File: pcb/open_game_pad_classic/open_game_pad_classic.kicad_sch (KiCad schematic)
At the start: 36 parts, among them J1 COM-09032, J2 COM-09032, J3 USB_C_Receptacle_USB2.0_14P, U1 MM74C923, U2 74HC4051

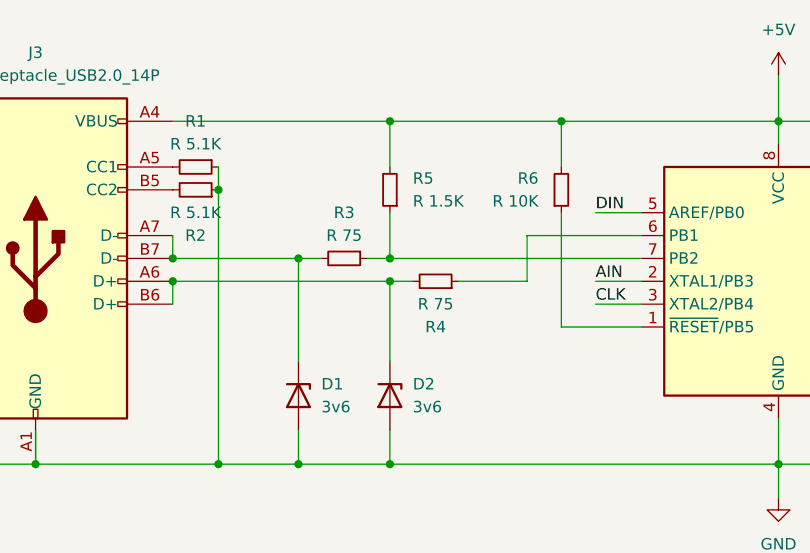
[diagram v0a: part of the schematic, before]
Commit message: Added more footprints for switches.
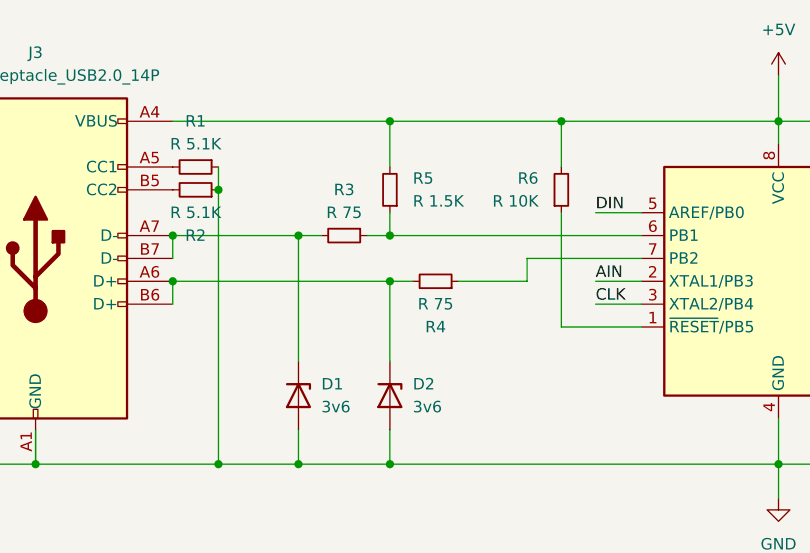
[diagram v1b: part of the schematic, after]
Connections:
- net at mC1.6 (PB1): now also R3.1, R5.1; no longer R4.1
- new net: R4.1, mC1.7 (PB2)
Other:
- moved on the sheet: R3
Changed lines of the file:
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@@
 	)
 	(junction
-		(at 90.17 43.18)
+		(at 74.93 219.71)
 		(diameter 0)
 		(color 0 0 0 0)
 	)
 	(junction
-		(at 74.93 219.71)
+		(at 90.17 40.64)
 		(diameter 0)
 		(color 0 0 0 0)
@@
 	)
 	(junction
-		(at 66.04 43.18)
-		(diameter 0)
-		(color 0 0 0 0)
-	)
-	(junction
-		(at 80.01 43.18)
-		(diameter 0)
-		(color 0 0 0 0)
-	)
-	(junction
 		(at 158.75 204.47)
 		(diameter 0)
@@
 	)
 	(junction
+		(at 66.04 40.64)
+		(diameter 0)
+		(color 0 0 0 0)
+	)
+	(junction
 		(at 177.8 242.57)
 		(diameter 0)
@@
 	)
 	(junction
+		(at 80.01 40.64)
+		(diameter 0)
+		(color 0 0 0 0)
+	)
+	(junction
 		(at 128.27 143.51)
 		(diameter 0)
@@
 	(wire
 		(pts
+			(xy 80.01 40.64) (xy 80.01 54.61)
+		)
+		(stroke
+			(width 0)
+			(type default)
+		)
+	)
+	(wire
+		(pts
 			(xy 20.32 226.06) (xy 30.48 226.06)
 		)
@@
 	(wire
 		(pts
+			(xy 105.41 43.18) (xy 118.11 43.18)
+		)
+		(stroke
+			(width 0)
+			(type default)
+		)
+	)
+	(wire
+		(pts
 			(xy 90.17 62.23) (xy 90.17 66.04)
 		)
@@
 	(wire
 		(pts
-			(xy 90.17 43.18) (xy 87.63 43.18)
+			(xy 90.17 40.64) (xy 87.63 40.64)
 		)
 		(stroke
@@
 	(wire
 		(pts
-			(xy 80.01 43.18) (xy 80.01 54.61)
-		)
-		(stroke
-			(width 0)
-			(type default)
-		)
-	)
-	(wire
-		(pts
 			(xy 68.58 104.14) (xy 90.17 104.14)
 		)
@@
 	(wire
 		(pts
-			(xy 80.01 43.18) (xy 66.04 43.18)
-		)
-		(stroke
-			(width 0)
-			(type default)
-		)
-	)
-	(wire
-		(pts
-			(xy 90.17 43.18) (xy 118.11 43.18)
+			(xy 80.01 40.64) (xy 66.04 40.64)
 		)
 		(stroke
@@
 	(wire
 		(pts
-			(xy 105.41 40.64) (xy 118.11 40.64)
-		)
-		(stroke
-			(width 0)
-			(type default)
-		)
-	)
-	(wire
-		(pts
 			(xy 40.64 219.71) (xy 40.64 231.14)
 		)
@@
 	(wire
 		(pts
+			(xy 105.41 45.72) (xy 105.41 43.18)
+		)
+		(stroke
+			(width 0)
+			(type default)
+		)
+	)
+	(wire
+		(pts
 			(xy 130.81 143.51) (xy 128.27 143.51)
 		)
@@
 	(wire
 		(pts
-			(xy 82.55 43.18) (xy 80.01 43.18)
+			(xy 82.55 40.64) (xy 80.01 40.64)
 		)
 		(stroke
@@
 	(wire
 		(pts
-			(xy 90.17 38.1) (xy 90.17 43.18)
+			(xy 90.17 38.1) (xy 90.17 40.64)
 		)
 		(stroke
@@
 	(wire
 		(pts
+			(xy 90.17 40.64) (xy 118.11 40.64)
+		)
+		(stroke
+			(width 0)
+			(type default)
+		)
+	)
+	(wire
+		(pts
 			(xy 40.64 182.88) (xy 40.64 196.85)
 		)
@@
 	(wire
 		(pts
-			(xy 105.41 45.72) (xy 105.41 40.64)
-		)
-		(stroke
-			(width 0)
-			(type default)
-		)
-	)
-	(wire
-		(pts
 			(xy 68.58 158.75) (xy 80.01 158.75)
 		)
@@
 	(symbol
 		(lib_id "Device:R_Small")
-		(at 85.09 43.18 270)
+		(at 85.09 40.64 270)
 		(unit 1)
 		(exclude_from_sim no)
@@
 		(fields_autoplaced yes)
 		(property "Reference" "R3"
-			(at 85.09 38.1 90)
+			(at 85.09 35.56 90)
 			(effects
 				(font
@@
 		)
 		(property "Value" "R 75"
-			(at 85.09 40.64 90)
+			(at 85.09 38.1 90)
 			(effects
 				(font
@@
 		)
 		(property "Footprint" ""
-			(at 85.09 43.18 0)
+			(at 85.09 40.64 0)
 			(effects
 				(font
@@
 		)
 		(property "Datasheet" "~"
-			(at 85.09 43.18 0)
+			(at 85.09 40.64 0)
 			(effects
 				(font
@@
 		)
 		(property "Description" "Resistor, small symbol"
-			(at 85.09 43.18 0)
+			(at 85.09 40.64 0)
 			(effects
 				(font

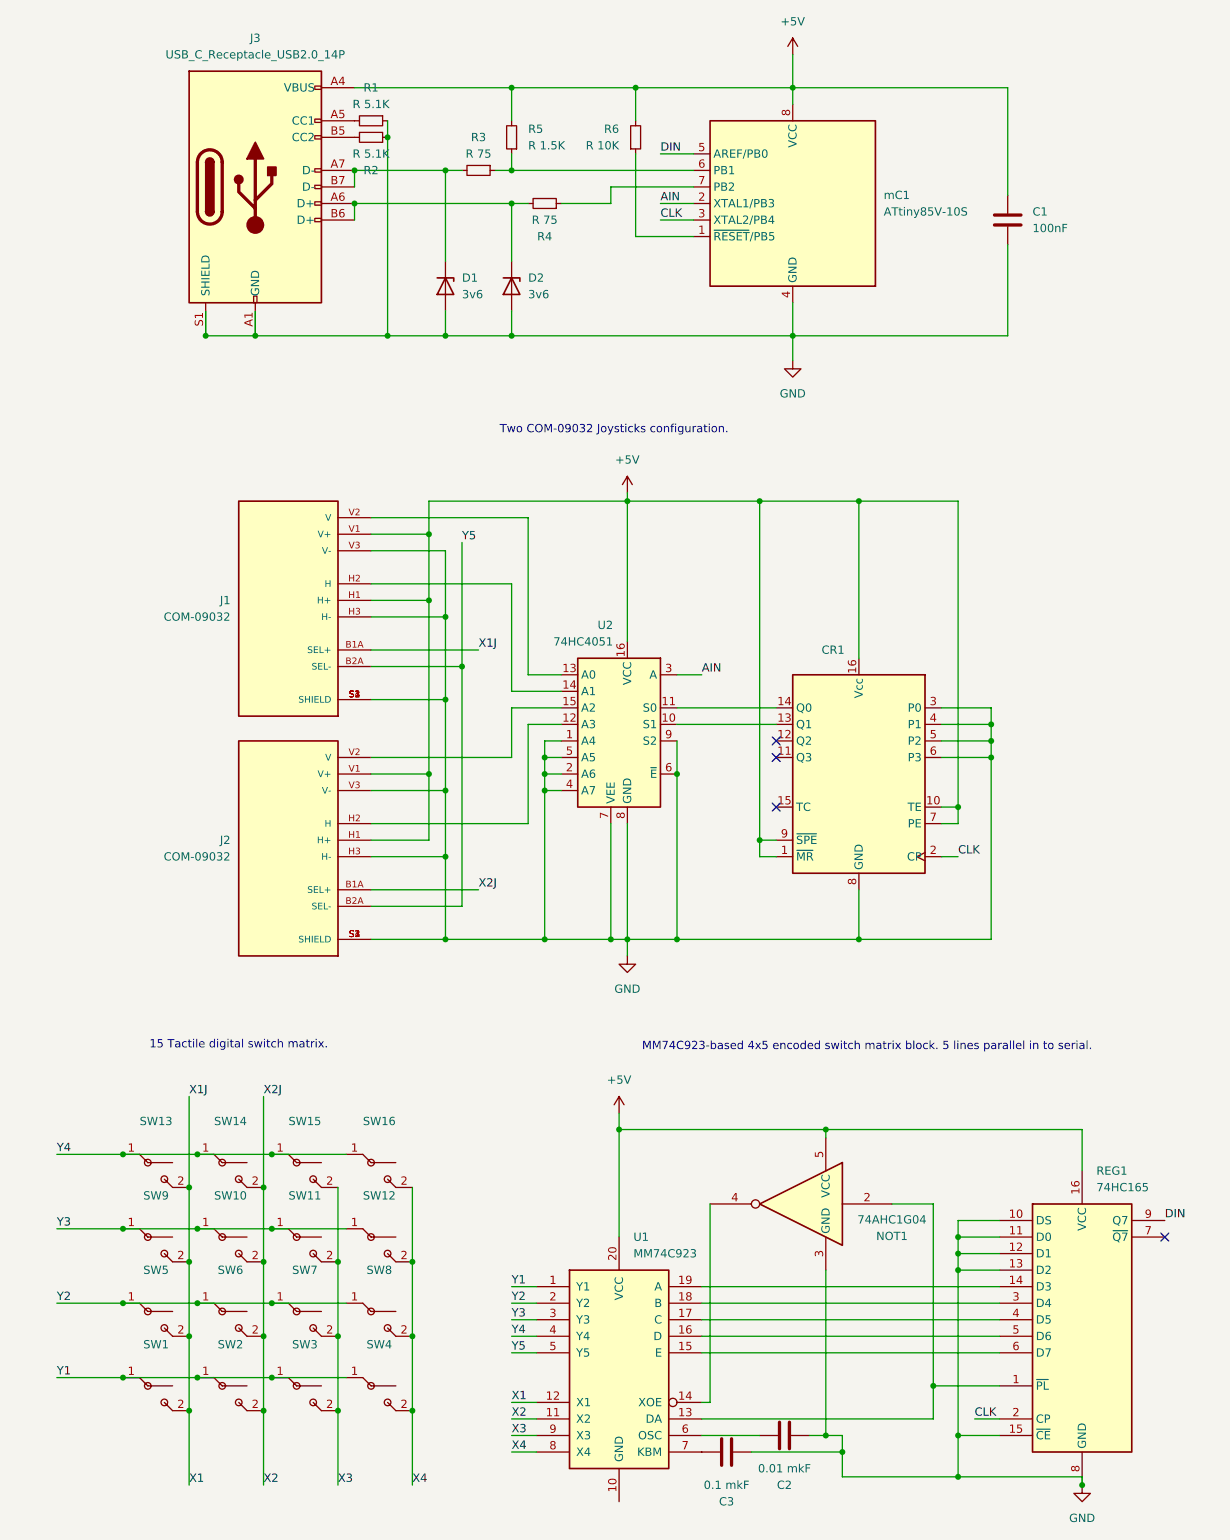
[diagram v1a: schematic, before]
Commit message: Added an inverting amplifier circuit to convert a -2.5V +2.5V signal to 0V - 5V for further use in ADC converter.
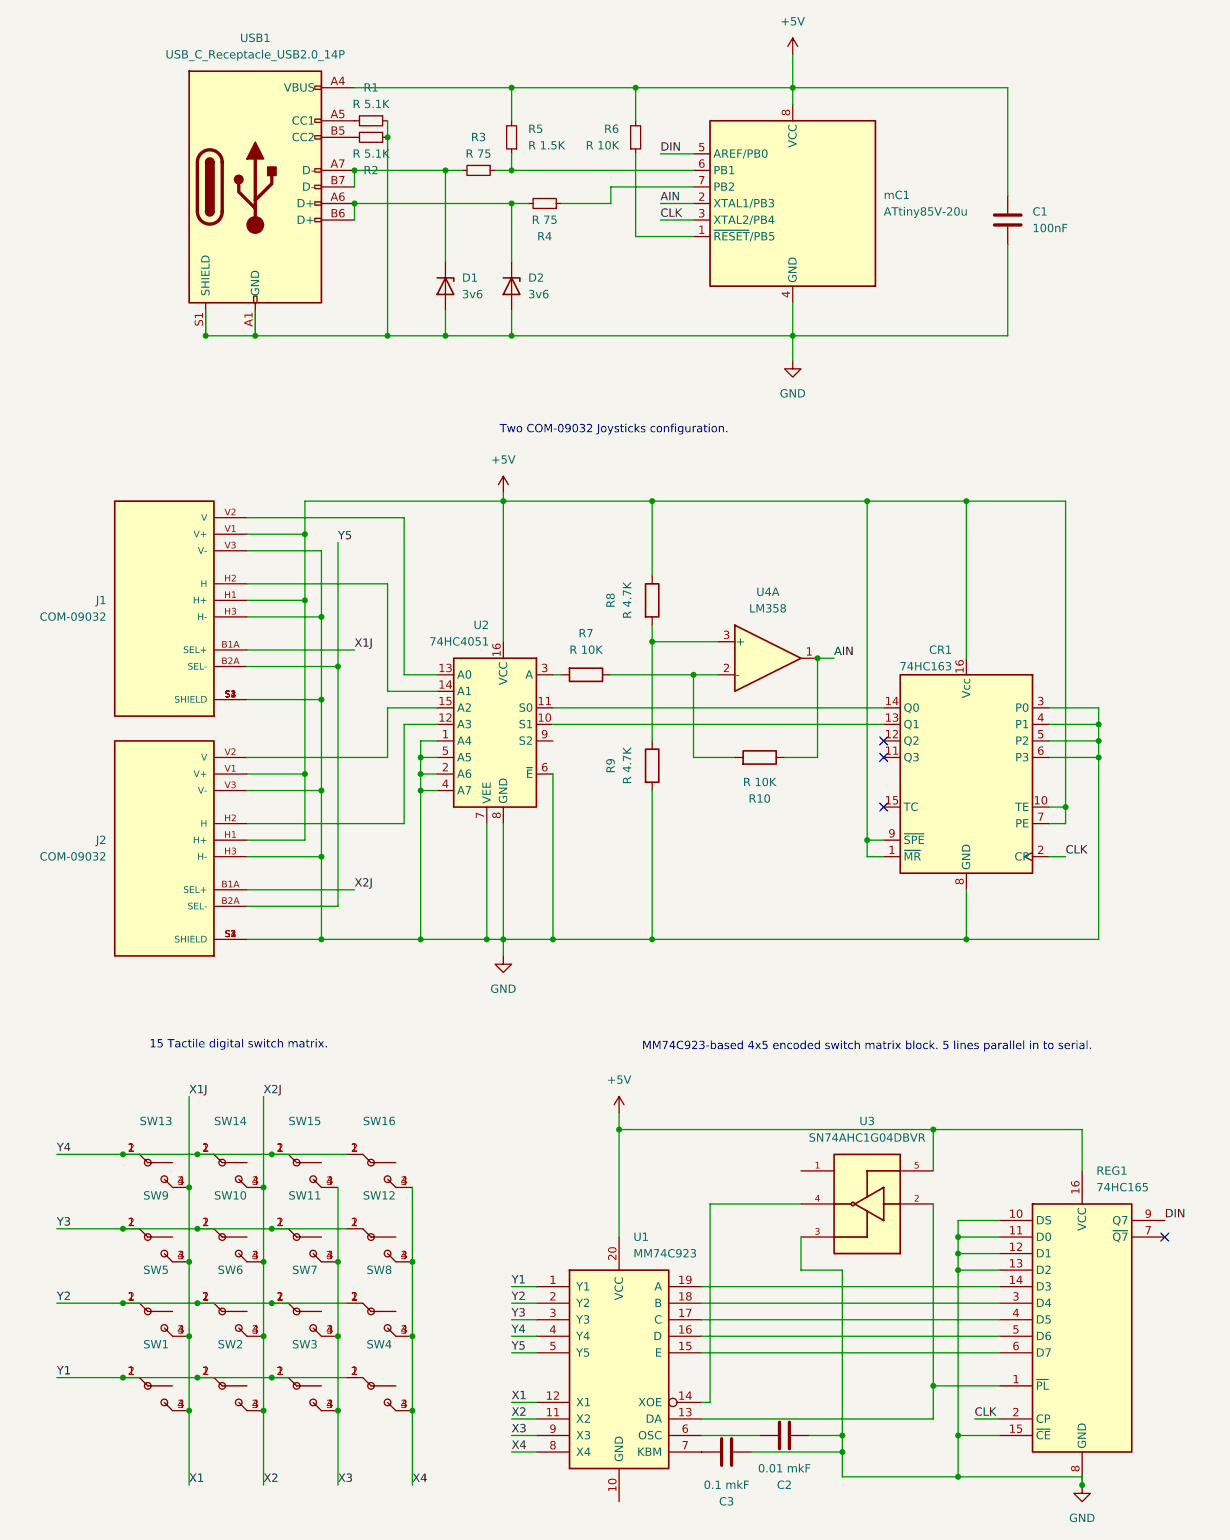
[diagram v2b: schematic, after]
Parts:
- removed NOT1: 74AHC1G04, Package_DIP:DIP-14_W7.62mm, symbol 74xGxx:74AHC1G04
- added R10, R7: R 10K, symbol Device:R
- added R8, R9: R 4.7K, symbol Device:R
- added U3: SN74AHC1G04DBVR, SN74AHC1G04DBVR:SOT95P280X145-5N, symbol SN74AHC1G04DBVR:SN74AHC1G04DBVR
- added U4: LM358, symbol Amplifier_Operational:LM358
- C1: footprint (none) -> Capacitor_SMD:C_01005_0402Metric
- C2, C3: footprint (none) -> Capacitor_SMD:C_0402_1005Metric
- CR1: value ~ -> 74HC163; footprint (none) -> Package_SO:SOIC-16W_7.5x10.3mm_P1.27mm
- R1, R5: footprint (none) -> Resistor_SMD:R_0603_1608Metric
- R2, R3, R4, R6: footprint (none) -> Resistor_SMD:R_0402_1005Metric
- REG1: footprint (none) -> Package_SO:SOIC-16_3.9x9.9mm_P1.27mm
- U1: footprint (none) -> Package_SO:SOIC-20W_7.5x12.8mm_P1.27mm
- U2: footprint (none) -> Package_SO:TSSOP-16_4.4x5mm_P0.65mm
- USB1: renamed from J3; footprint (none) -> Connector_USB:USB_C_Receptacle_HCTL_HC-TYPE-C-16P-01A
- mC1: value ATtiny85V-10S -> ATtiny85V-20u
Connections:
- net +5V: now also R8.1, U3.5
- net AIN: now also R10.1, U4.1; no longer U2.3 (A)
- net GND: now also R9.2, U3.3; no longer U2.9 (S2)
- net X1: now also SW1.3 (B), SW1.4 (B), SW13.3 (B), SW13.4 (B), SW5.3 (B), SW5.4 (B), SW9.3 (B), SW9.4 (B); no longer SW1.2 (B), SW13.2 (B), SW5.2 (B), SW9.2 (B)
- net X2: now also SW10.3 (B), SW10.4 (B), SW14.3 (B), SW14.4 (B), SW2.3 (B), SW2.4 (B), SW6.3 (B), SW6.4 (B); no longer SW10.2 (B), SW14.2 (B), SW2.2 (B), SW6.2 (B)
- net X3: now also SW11.3 (B), SW11.4 (B), SW15.3 (B), SW15.4 (B), SW3.3 (B), SW3.4 (B), SW7.3 (B), SW7.4 (B); no longer SW11.2 (B), SW15.2 (B), SW3.2 (B), SW7.2 (B)
- net X4: now also SW12.3 (B), SW12.4 (B), SW16.3 (B), SW16.4 (B), SW4.3 (B), SW4.4 (B), SW8.3 (B), SW8.4 (B); no longer SW12.2 (B), SW16.2 (B), SW4.2 (B), SW8.2 (B)
- net Y1: now also SW1.2 (A), SW2.2 (A), SW3.2 (A), SW4.2 (A)
- net Y2: now also SW5.2 (A), SW6.2 (A), SW7.2 (A), SW8.2 (A)
- net Y3: now also SW10.2 (A), SW11.2 (A), SW12.2 (A), SW9.2 (A)
- net Y4: now also SW13.2 (A), SW14.2 (A), SW15.2 (A), SW16.2 (A)
- net at REG1.1 (~{PL}), U1.13 (DA): now also U3.2
- net at U1.14 (XOE): now also U3.4
- new net: R7.2, U2.3 (A)
- new net: R10.2, R7.1, U4.2 (-)
- new net: R8.2, R9.1, U4.3 (+)
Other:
- moved on the sheet: CR1, J1, J2

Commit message: Minor changes to register values and their footprint
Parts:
- C1: footprint Capacitor_SMD:C_01005_0402Metric -> Capacitor_SMD:C_0603_1608Metric
- R10: footprint (none) -> Resistor_SMD:R_0805_2012Metric
- R7, R8, R9: footprint (none) -> Resistor_SMD:R_0402_1005Metric
- U4: footprint (none) -> LM358:DIL8
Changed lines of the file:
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@@
 			)
 		)
-		(property "Footprint" ""
+		(property "Footprint" "LM358:DIL8"
 			(at 129.54 115.57 0)
 			(effects
@@
 			)
 		)
-		(property "Footprint" ""
+		(property "Footprint" "Resistor_SMD:R_0402_1005Metric"
 			(at 109.982 106.68 90)
 			(effects
@@
 			)
 		)
-		(property "Footprint" ""
+		(property "Footprint" "Resistor_SMD:R_0805_2012Metric"
 			(at 128.27 132.588 90)
 			(effects
@@
 			)
 		)
-		(property "Footprint" ""
+		(property "Footprint" "Resistor_SMD:R_0402_1005Metric"
 			(at 101.6 116.332 90)
 			(effects
@@
 			)
 		)
-		(property "Footprint" ""
+		(property "Footprint" "Resistor_SMD:R_0402_1005Metric"
 			(at 109.982 132.08 90)
 			(effects
@@
 			)
 		)
-		(property "Footprint" "Capacitor_SMD:C_01005_0402Metric"
+		(property "Footprint" "Capacitor_SMD:C_0603_1608Metric"
 			(at 167.3352 52.07 0)
 			(effects
